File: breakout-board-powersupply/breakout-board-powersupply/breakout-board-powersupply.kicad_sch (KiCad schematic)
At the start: 14 parts, among them J1 Screw_Terminal_01x02, T1 Transformer_1P_1S, U1 L7805

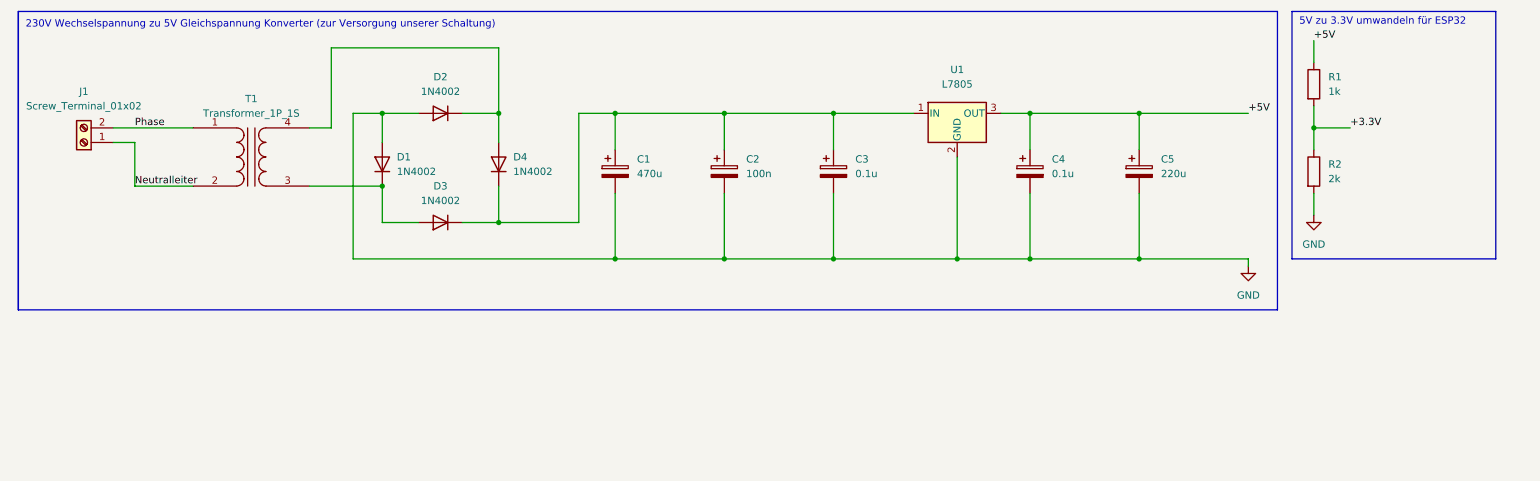
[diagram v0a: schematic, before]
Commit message: kicad datei für das powersupply breakout board wurde erstellt
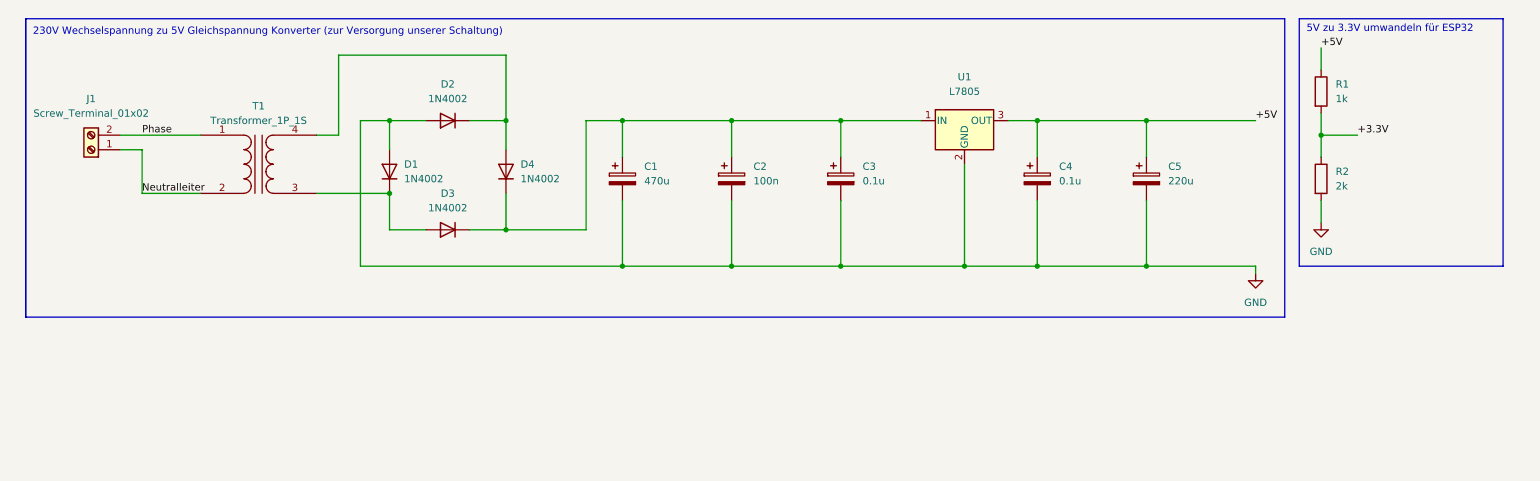
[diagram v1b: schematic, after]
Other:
- title: module-power-measurement -> (none)

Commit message: Das atTiny breajout board ist fertig!
Laci hat einige Dinge an den breakout boards geändert
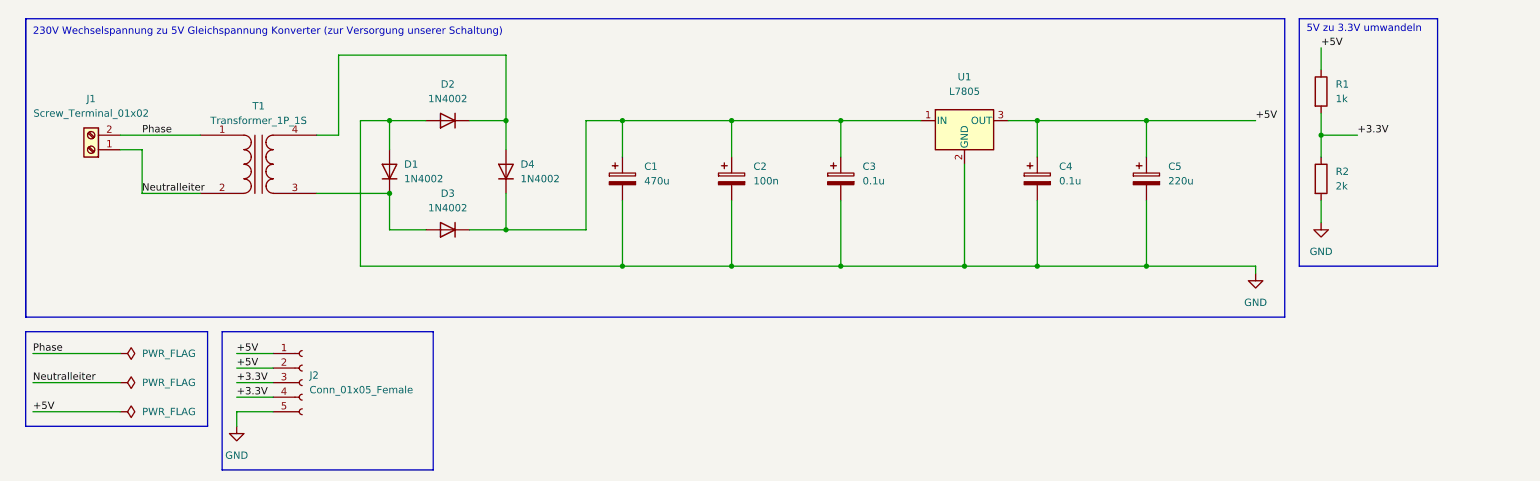
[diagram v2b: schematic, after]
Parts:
- added J2: Conn_01x05_Female, Connector_PinSocket_2.54mm:PinSocket_1x05_P2.54mm_Vertical, symbol Connector:Conn_01x05_Female
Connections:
- net +3.3V: now also J2.3 (Pin_3), J2.4 (Pin_4)
- net +5V: now also J2.1 (Pin_1), J2.2 (Pin_2)
- net GND: now also J2.5 (Pin_5)
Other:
- note added: "5V zu 3.3V umwandeln"
- note removed: "5V zu 3.3V umwandeln für ESP32"
- title: (none) -> breakout-board-powersupply

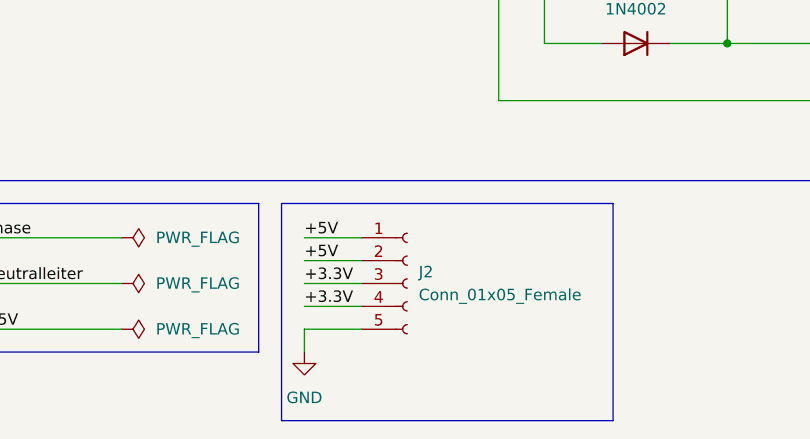
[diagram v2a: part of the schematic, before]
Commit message: KiCad 7.0
Updated to KiCad 7.0 file format
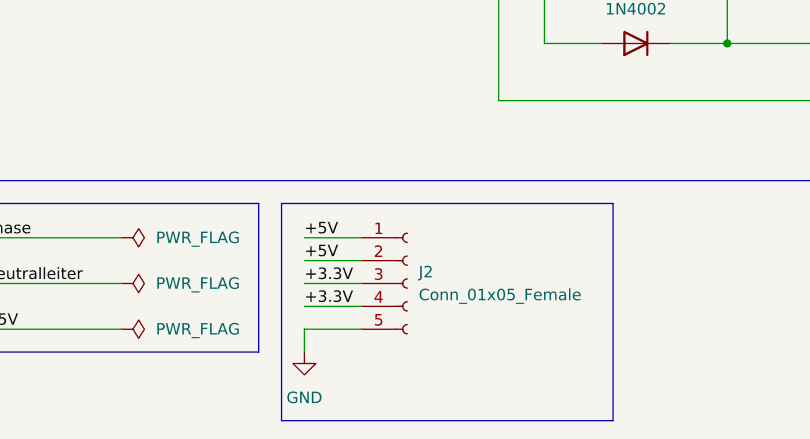
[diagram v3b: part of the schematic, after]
